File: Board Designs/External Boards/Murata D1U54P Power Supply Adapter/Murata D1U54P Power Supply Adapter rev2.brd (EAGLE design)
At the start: 45.5 x 54.9 mm, 21 parts, among them X1 CONNECTOR-2, X2 CONNECTOR-2NANO-FIT_VERTICAL-2, X3 CONNECTOR-2, X4 CONNECTOR-2

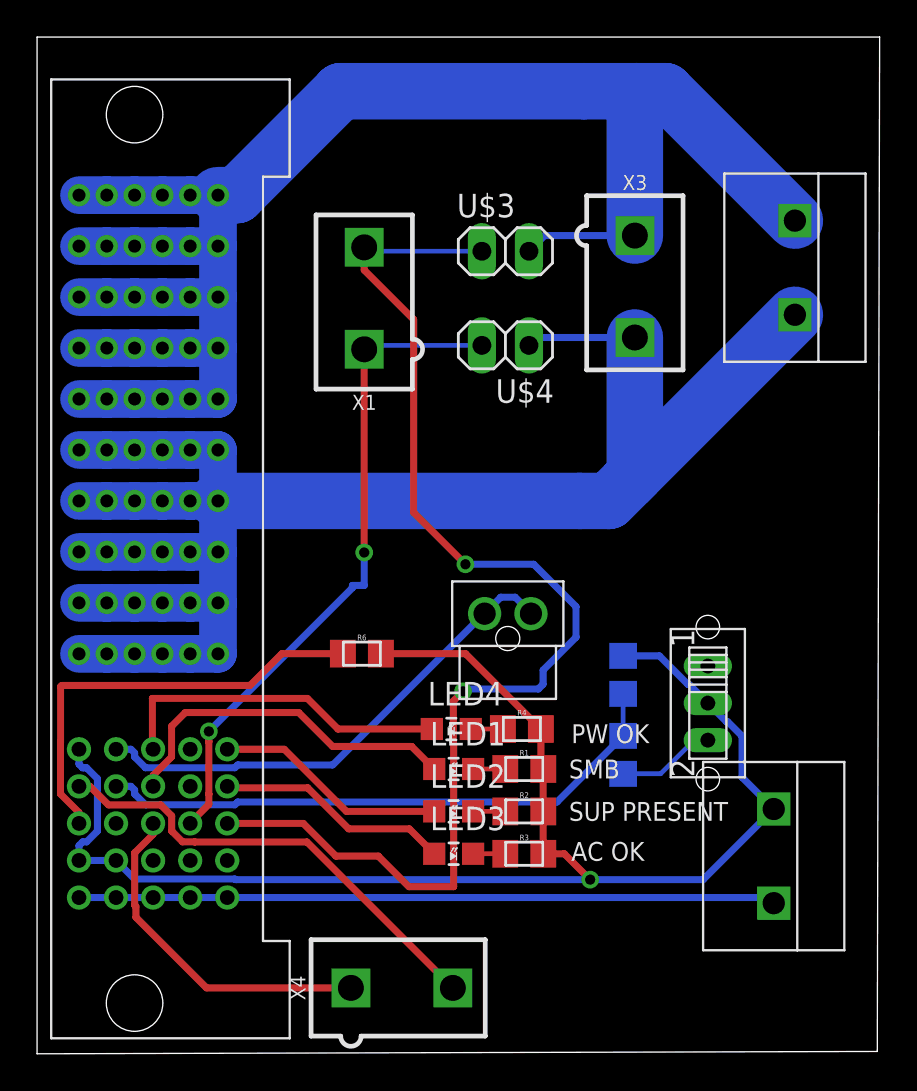
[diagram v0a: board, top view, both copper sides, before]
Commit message: Reverted to clean version for CAN_Tester
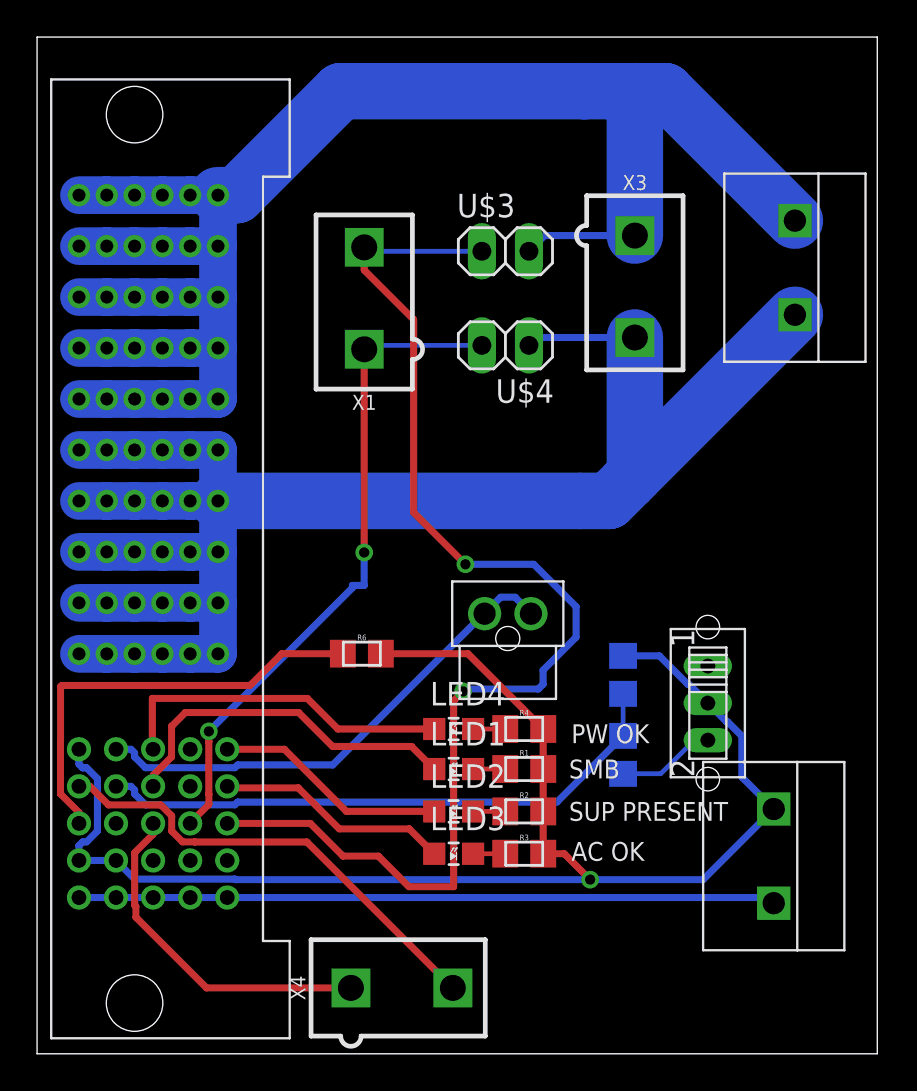
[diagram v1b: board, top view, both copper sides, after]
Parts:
- moved R4 0.13 mm to (27.6, 17.5)
- moved LED4 0.13 mm to (23.7, 17.5)
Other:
- board size 45.5 x 54.9 mm -> 45.3 x 54.9 mm
- board text added: "2019 Murata D1U54P adapter rev2"
